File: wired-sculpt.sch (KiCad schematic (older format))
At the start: 39 parts, among them J1 10103594-0001LF, J2 FFC3B07-30-T, J3 AVR-ISP-6 - NOT FITTED, Q1 BSS84AK,215, Q2 2N7002BK, SW1 FSMSM, SW2 S2B-PH-K-S(LF)(SN), U1 USBLC6-2SC6, U2 LM2776DBVT, U3 AT90USB1286-AU, Y1 TSX-3225 16.0000MF18X-AC0

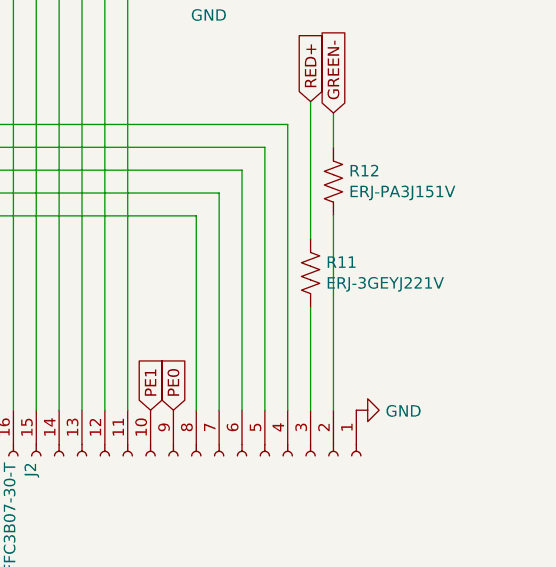
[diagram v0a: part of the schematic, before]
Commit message: set red and green current-limiting resistors to 150R
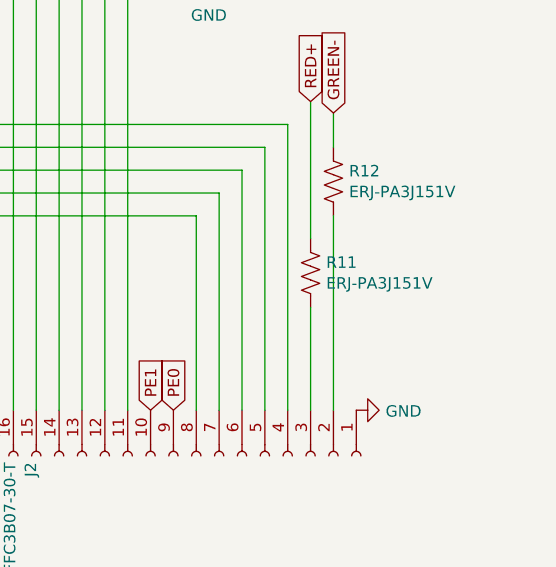
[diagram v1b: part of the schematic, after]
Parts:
- R11: value ERJ-3GEYJ221V -> ERJ-PA3J151V; Notes (none) -> Allows 10 mA. Maybe 100R would be fine.
- R12: Notes (none) -> Measures at 15-17 mA.
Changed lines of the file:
@@
 P 9350 5350
 F 0 "R11" H 9418 5396 50  0000 L CNN
-F 1 "ERJ-3GEYJ221V" H 9418 5305 50  0000 L CNN
+F 1 "ERJ-PA3J151V" H 9418 5305 50  0000 L CNN
 F 2 "Resistor_SMD:R_0603_1608Metric" V 9390 5340 50  0001 C CNN
 F 3 "~" H 9350 5350 50  0001 C CNN
+F 4 "Allows 10 mA. Maybe 100R would be fine." H 9350 5350 50  0001 C CNN "Notes"
 	1    9350 5350
 	1    0    0    -1
@@
 F 2 "Resistor_SMD:R_0603_1608Metric" V 9490 4940 50  0001 C CNN
 F 3 "~" H 9450 4950 50  0001 C CNN
+F 4 "Measures at 15-17 mA." H 9450 4950 50  0001 C CNN "Notes"
 	1    9450 4950
 	1    0    0    -1
